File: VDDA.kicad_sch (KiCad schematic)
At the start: 44 parts, among them J5 Conn_01x02, Q1 AO3401A, U6 L78M05ABDT-TR

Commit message: Fixed a lot more mistakes...
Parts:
- removed e10: SGM2205-ADJXTDB8G/TR, Package_DFN_QFN:DFN-8-1EP_3x3mm_P0.65mm_EP1.55x2.4mm, symbol Regulator_Linear:ADP7142AUJZ
- added e4: SGM2205-ADJXTDB8G/TR, Package_DFN_QFN:DFN-8-1EP_3x3mm_P0.65mm_EP1.55x2.4mm, symbol Regulator_Linear:ADP7142AUJZ
- TP25, TP26, TP27: footprint TP_Label:TestPoint_THTPad_D2.0mm_Drill1.0mm -> TestPoint:TestPoint_THTPad_D2.5mm_Drill1.2mm
- e1: Price (none) -> $0.76
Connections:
- net GND: now also e4.7 (GND), e4.9 (PAD)
- net at C87.2, R10.1, R24.1: now also e4.6 (SENSE/ADJ)
- net at C87.1, C88.1, R24.2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: now also e4.3 (VOUT), e4.4 (VOUT)
- net at C85.1, C86.1, FB8.2: now also e4.1 (VIN), e4.2 (VIN), e4.8 (EN)
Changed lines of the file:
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@@
 	)
 	(junction
-		(at 138.43 135.89)
+		(at 162.56 138.43)
 		(diameter 0)
 		(color 0 0 0 0)
 	)
 	(junction
-		(at 162.56 138.43)
+		(at 138.43 135.89)
 		(diameter 0)
 		(color 0 0 0 0)
 	)
 	(junction
-		(at 132.08 100.33)
+		(at 152.4 146.05)
 		(diameter 0)
 		(color 0 0 0 0)
 	)
 	(junction
-		(at 142.24 135.89)
+		(at 132.08 100.33)
 		(diameter 0)
 		(color 0 0 0 0)
@@
 	)
 	(junction
-		(at 152.4 146.05)
+		(at 142.24 135.89)
 		(diameter 0)
 		(color 0 0 0 0)
@@
 			)
 		)
-		(property "Footprint" "TP_Label:TestPoint_THTPad_D2.0mm_Drill1.0mm"
+		(property "Footprint" "TestPoint:TestPoint_THTPad_D2.5mm_Drill1.2mm"
 			(at 233.68 140.97 0)
 			(hide yes)
@@
 			)
 		)
-		(property "Footprint" "TP_Label:TestPoint_THTPad_D2.0mm_Drill1.0mm"
+		(property "Footprint" "TestPoint:TestPoint_THTPad_D2.5mm_Drill1.2mm"
 			(at 233.68 105.41 0)
 			(hide yes)
@@
 	)
 	(symbol
-		(lib_name "ADP7142AUJZ_1")
-		(lib_id "Regulator_Linear:ADP7142AUJZ")
-		(at 152.4 138.43 0)
-		(unit 1)
-		(body_style 1)
-		(exclude_from_sim no)
-		(in_bom yes)
-		(on_board yes)
-		(in_pos_files yes)
-		(dnp no)
-		(fields_autoplaced yes)
-		(property "Reference" "e10"
-			(at 152.4 128.27 0)
-			(show_name no)
-			(do_not_autoplace no)
-			(effects
-				(font
-					(size 1.27 1.27)
-				)
-			)
-		)
-		(property "Value" "SGM2205-ADJXTDB8G/TR"
-			(at 152.4 130.81 0)
-			(show_name no)
-			(do_not_autoplace no)
-			(effects
-				(font
-					(size 1.27 1.27)
-				)
-			)
-		)
-		(property "Footprint" "Package_DFN_QFN:DFN-8-1EP_3x3mm_P0.65mm_EP1.55x2.4mm"
-			(at 152.4 148.59 0)
-			(hide yes)
-			(show_name no)
-			(do_not_autoplace no)
-			(effects
-				(font
-					(size 1.27 1.27)
-					(italic yes)
-				)
-			)
-		)
-		(property "Datasheet" "https://jlcpcb.com/api/file/downloadByFileSystemAccessId/8590903048351141888"
-			(at 152.4 151.13 0)
-			(hide yes)
-			(show_name no)
-			(do_not_autoplace no)
-			(effects
-				(font
-					(size 1.27 1.27)
-				)
-			)
-		)
-		(property "Description" "300mA, Low Noise,  Low Dropout Regulator, Positive, Adjustable, TSOT-23-5"
-			(at 152.4 138.43 0)
-			(hide yes)
-			(show_name no)
-			(do_not_autoplace no)
-			(effects
-				(font
-					(size 1.27 1.27)
-				)
-			)
-		)
-		(property "LCSC" "C5152847"
-			(at 152.4 138.43 0)
-			(hide yes)
-			(show_name no)
-			(do_not_autoplace no)
-			(effects
-				(font
-					(size 1.27 1.27)
-				)
-			)
-		)
-		(pin "7"
-		)
-		(pin "6"
-		)
-		(pin "8"
-		)
-		(pin "1"
-		)
-		(pin "4"
-		)
-		(pin "3"
-		)
-		(pin "2"
-		)
-		(pin "5"
-		)
-		(pin "9"
-		)
-		(instances
-			(project "DDC_SDR"
-				(path "/7dfef218-ca21-47b0-a8d3-67c7d55cb9d2/48946e56-e004-4035-9a82-30e09af92ded"
-					(reference "e10")
-					(unit 1)
-				)
-			)
-		)
-	)
-	(symbol
 		(lib_id "Jumper:Jumper_2_Open")
 		(at 176.53 50.8 0)
@@
 	)
 	(symbol
+		(lib_name "ADP7142AUJZ_1")
+		(lib_id "Regulator_Linear:ADP7142AUJZ")
+		(at 152.4 138.43 0)
+		(unit 1)
+		(body_style 1)
+		(exclude_from_sim no)
+		(in_bom yes)
+		(on_board yes)
+		(in_pos_files yes)
+		(dnp no)
+		(fields_autoplaced yes)
+		(property "Reference" "e4"
+			(at 152.4 128.27 0)
+			(show_name no)
+			(do_not_autoplace no)
+			(effects
+				(font
+					(size 1.27 1.27)
+				)
+			)
+		)
+		(property "Value" "SGM2205-ADJXTDB8G/TR"
+			(at 152.4 130.81 0)
+			(show_name no)
+			(do_not_autoplace no)
+			(effects
+				(font
+					(size 1.27 1.27)
+				)
+			)
+		)
+		(property "Footprint" "Package_DFN_QFN:DFN-8-1EP_3x3mm_P0.65mm_EP1.55x2.4mm"
+			(at 152.4 148.59 0)
+			(hide yes)
+			(show_name no)
+			(do_not_autoplace no)
+			(effects
+				(font
+					(size 1.27 1.27)
+					(italic yes)
+				)
+			)
+		)
+		(property "Datasheet" "https://jlcpcb.com/api/file/downloadByFileSystemAccessId/8590903048351141888"
+			(at 152.4 151.13 0)
+			(hide yes)
+			(show_name no)
+			(do_not_autoplace no)
+			(effects
+				(font
+					(size 1.27 1.27)
+				)
+			)
+		)
+		(property "Description" "300mA, Low Noise,  Low Dropout Regulator, Positive, Adjustable, TSOT-23-5"
+			(at 152.4 138.43 0)
+			(hide yes)
+			(show_name no)
+			(do_not_autoplace no)
+			(effects
+				(font
+					(size 1.27 1.27)
+				)
+			)
+		)
+		(property "LCSC" "C5152847"
+			(at 152.4 138.43 0)
+			(hide yes)
+			(show_name no)
+			(do_not_autoplace no)
+			(effects
+				(font
+					(size 1.27 1.27)
+				)
+			)
+		)
+		(property "Price" "$0.76"
+			(at 152.4 138.43 0)
+			(hide yes)
+			(show_name no)
+			(do_not_autoplace no)
+			(effects
+				(font
+					(size 1.27 1.27)
+				)
+			)
+		)
+		(pin "7"
+		)
+		(pin "6"
+		)
+		(pin "8"
+		)
+		(pin "1"
+		)
+		(pin "4"
+		)
+		(pin "3"
+		)
+		(pin "2"
+		)
+		(pin "5"
+		)
+		(pin "9"
+		)
+		(instances
+			(project "DDC_SDR"
+				(path "/7dfef218-ca21-47b0-a8d3-67c7d55cb9d2/48946e56-e004-4035-9a82-30e09af92ded"
+					(reference "e4")
+					(unit 1)
+				)
+			)
+		)
+	)
+	(symbol
 		(lib_id "PCM_JLCPCB-Resistors:0805,1Ω")
 		(at 193.04 135.89 90)
@@
 			)
 		)
-		(property "Footprint" "TP_Label:TestPoint_THTPad_D2.0mm_Drill1.0mm"
+		(property "Footprint" "TestPoint:TestPoint_THTPad_D2.5mm_Drill1.2mm"
 			(at 62.23 95.25 0)
 			(hide yes)
@@
 			(at 146.05 102.87 0)
 			(hide yes)
+			(show_name no)
+			(do_not_autoplace no)
+			(effects
+				(font
+					(size 1.27 1.27)
+				)
+			)
+		)
+		(property "Price" "$0.76"
+			(at 146.05 102.87 0)
+			(hide yes)

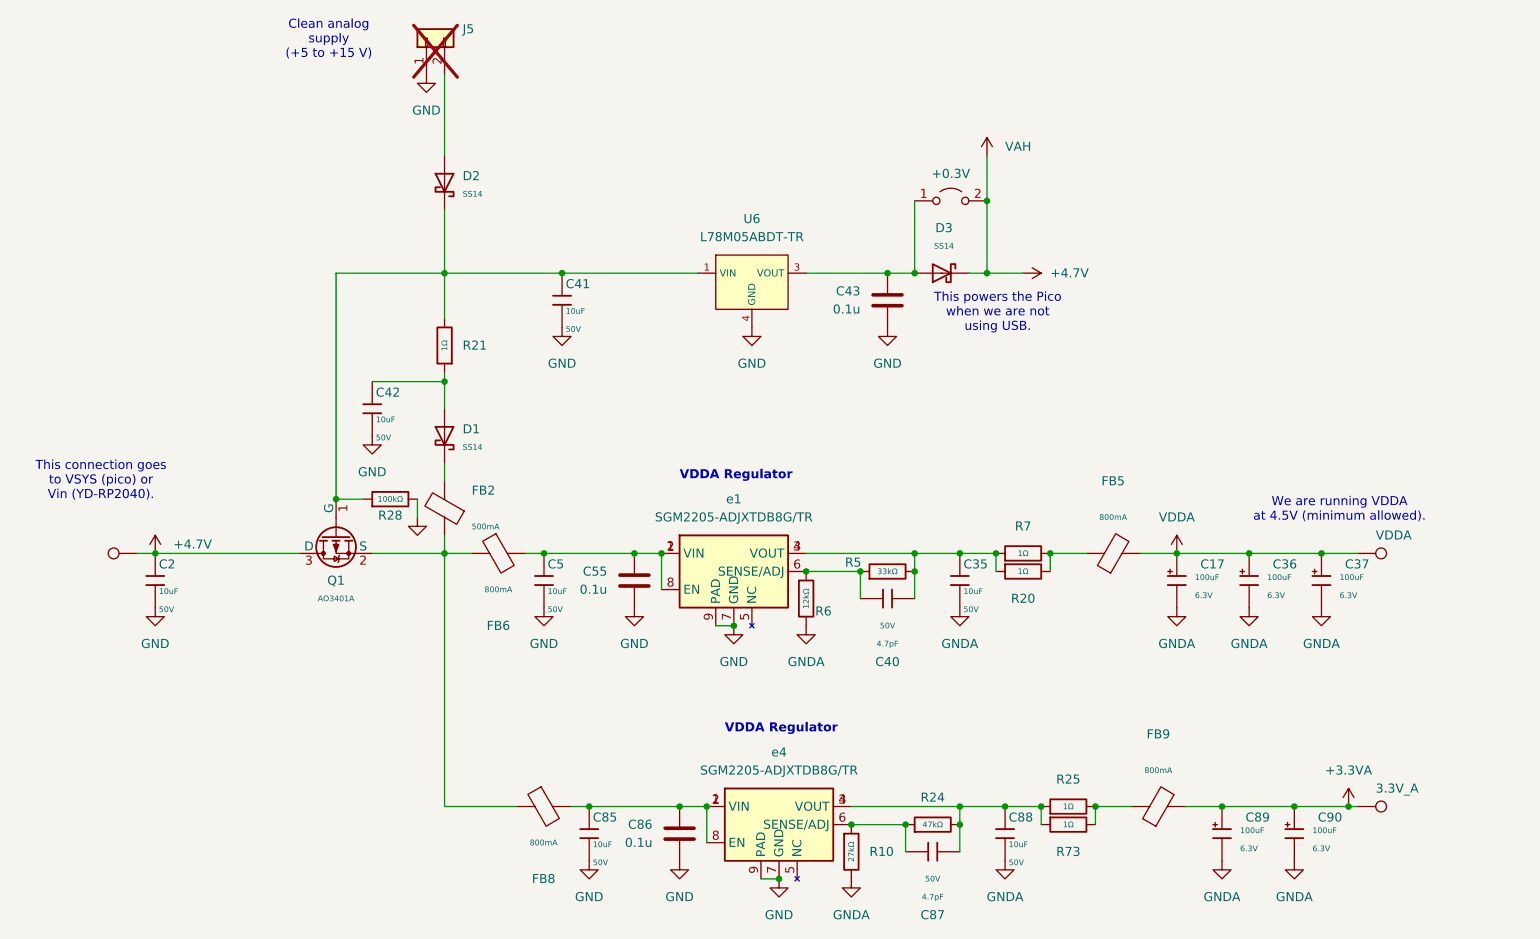
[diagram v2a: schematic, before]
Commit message: Starting to place components
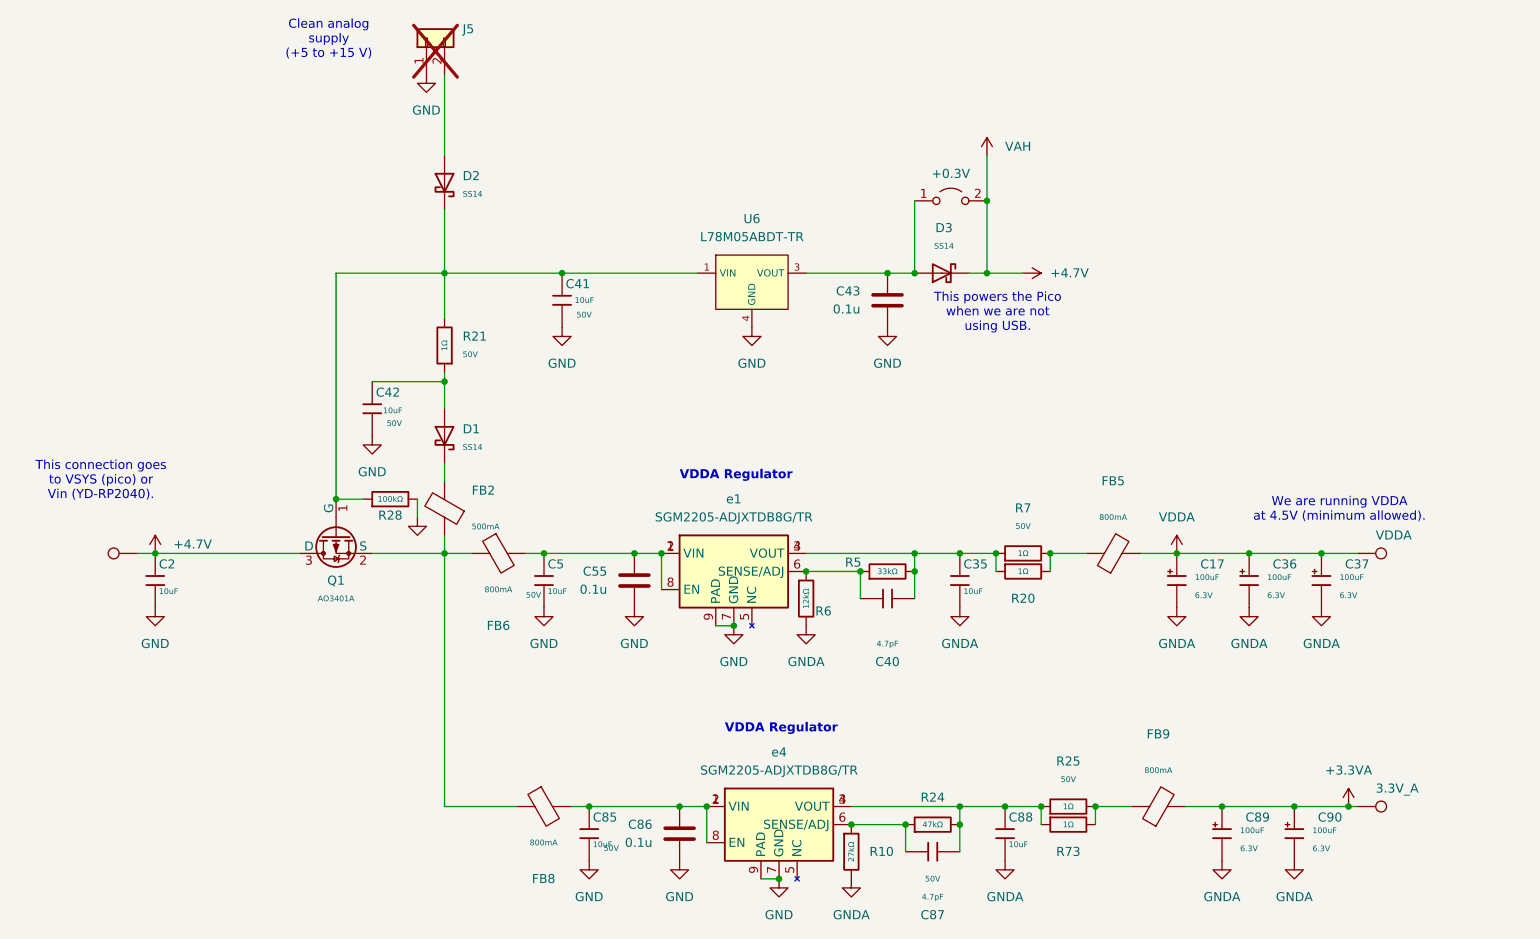
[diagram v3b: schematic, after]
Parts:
- C2, C35, C41, C42, C5, C85, C88: footprint PCM_JLCPCB:C_1206 -> PCM_JLCPCB:C_0805; symbol PCM_JLCPCB-Capacitors:1206,10uF -> PCM_JLCPCB-Capacitors:0805,10uF,(2); LCSC C13585 -> C440198; Manufacturer (none) -> Murata Electronics; Part CL31A106KBHNNNE -> GRM21BR61H106KE43L; Price 0.035USD -> 0.066USD; Stock 3698334 -> 1422246
- R20, R21, R25, R7, R73: footprint PCM_JLCPCB:R_0805 -> PCM_JLCPCB:R_0402; symbol PCM_JLCPCB-Resistors:0805,1Ω -> PCM_JLCPCB-Resistors:0402,1Ω; Capacitance (none) -> 10uF; Class Basic Component -> Preferred Component; LCSC C25271 -> C25086; Manufacturer (none) -> UNI-ROYAL(Uniroyal Elec); Overload Voltage (Max) 150V -> 50V; Part 0805W8F100KT5E -> 0402WGF100KTCE; Power(Watts) 125mW -> 62.5mW; Price 0.006USD -> 0.004USD; Stock 413540 -> 305976; Temperature Coefficient ±400ppm/°C -> ±200ppm/°C; Voltage Rated (none) -> 50V

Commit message: AF DAC Some VDDA Placed
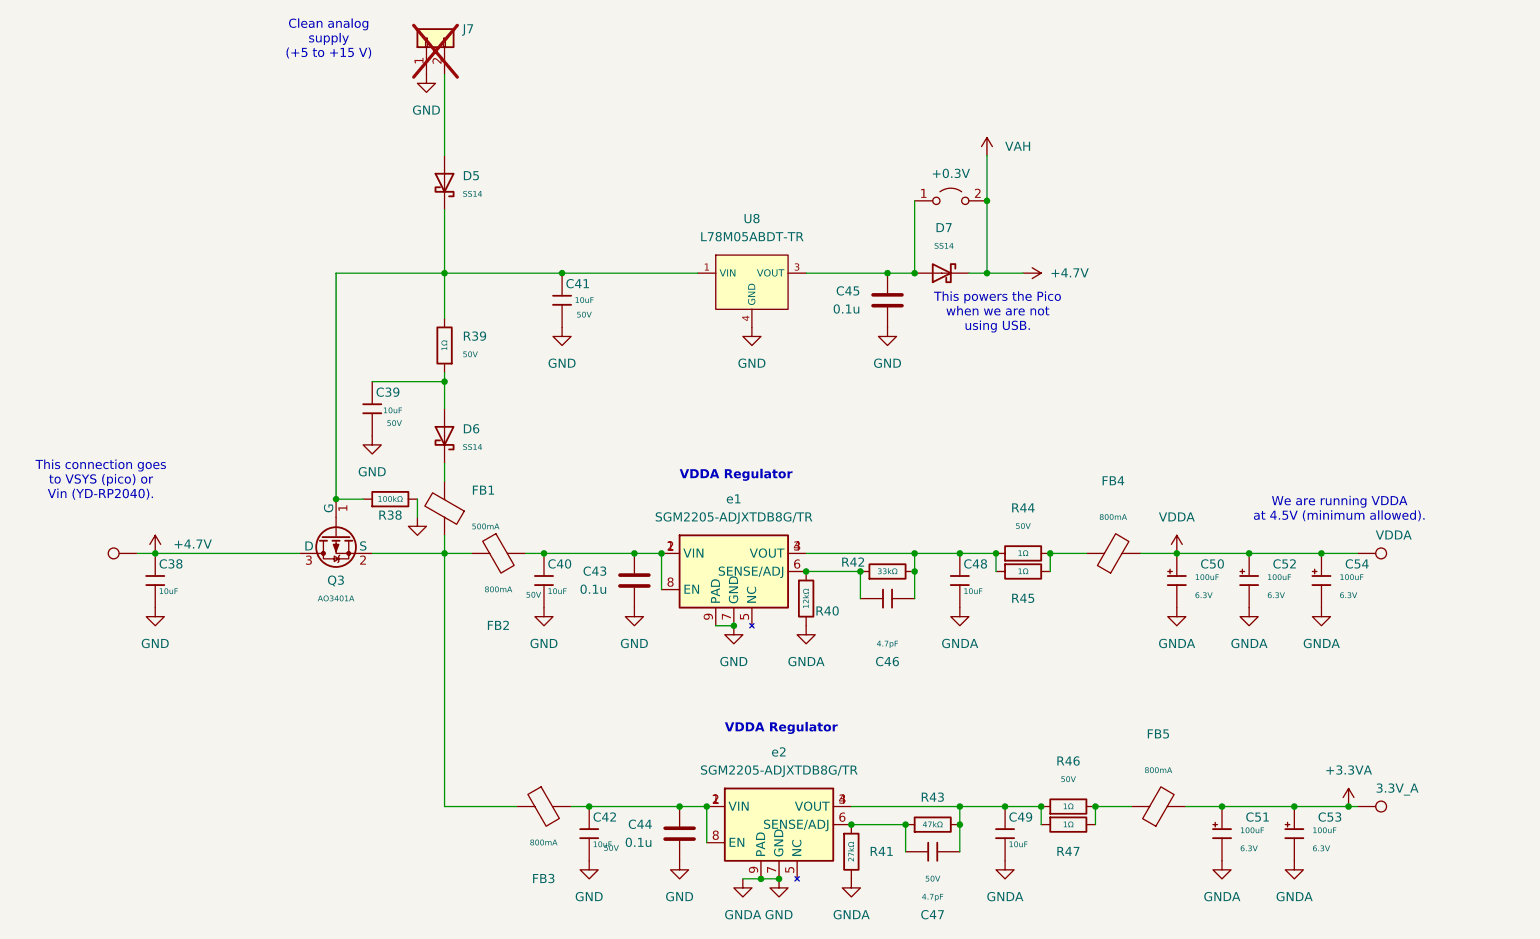
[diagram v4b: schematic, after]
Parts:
- renumbered C2 to C38, C42 to C39, C5 to C40, C85 to C42, C55 to C43, C86 to C44, C43 to C45, C40 to C46, C87 to C47, C35 to C48, C88 to C49, C17 to C50, C89 to C51, C36 to C52, C90 to C53, C37 to C54, D2 to D5, D1 to D6, D3 to D7, FB2 to FB1, FB6 to FB2, FB8 to FB3, FB5 to FB4, FB9 to FB5, J5 to J7, JP2 to JP5, Q1 to Q3, R28 to R38, R21 to R39, R6 to R40, R10 to R41, R5 to R42, R24 to R43, R7 to R44, R20 to R45, R25 to R46, R73 to R47, TP25 to TP4, TP26 to TP5, TP27 to TP6, U6 to U8, e4 to e2
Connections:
- net GNDA is gone; now on net GND: C48.2, C49.2, C50.2, C51.2, C52.2, C53.2, C54.2, R40.2, R41.2

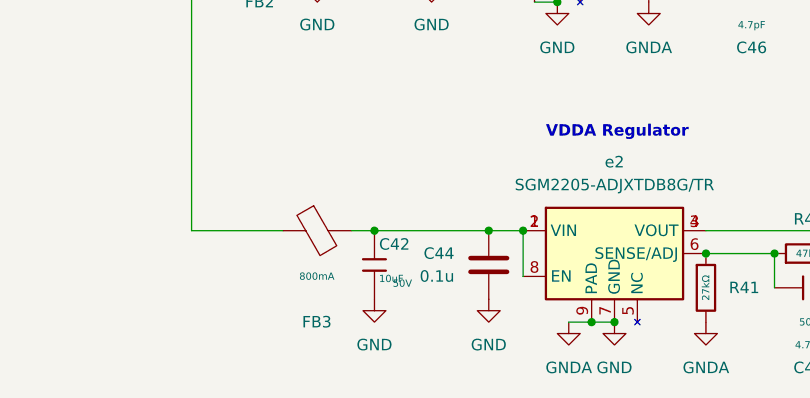
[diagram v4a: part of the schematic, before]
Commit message: SMA/LogicAnalyzer and VDDA placed
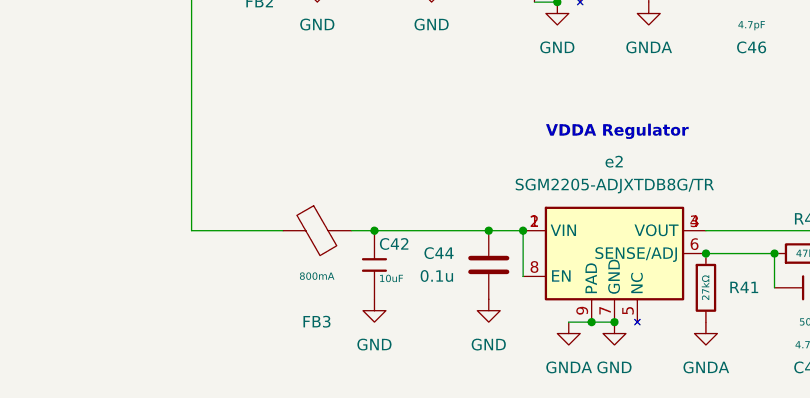
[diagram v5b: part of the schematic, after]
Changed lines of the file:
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@@
 		(property "Voltage Rated" "50V"
 			(at 127.762 141.7462 0)
+			(hide yes)
 			(show_name no)
 			(do_not_autoplace no)
